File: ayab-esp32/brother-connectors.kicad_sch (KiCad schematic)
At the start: 21 parts, among them J401 900_SOLENOIDS_A, J402 900_SOLENOIDS_B, J403 USER_I2C, J404 USER_SPI, J405 910_SOLENOIDS_A, J406 910_SOLENOIDS_B, J407 910_ENCODERS_EOL_R, J408 USER_UART, J409 930_SOLENOIDS_A, J410 930_SOLENOIDS_B, J411 930_910_EOL_L, J412 930_EOL_R, J413 930_ENCODERS, J414 965_EOL_L, J415 965_EOL_R, J416 965_ENCODERS

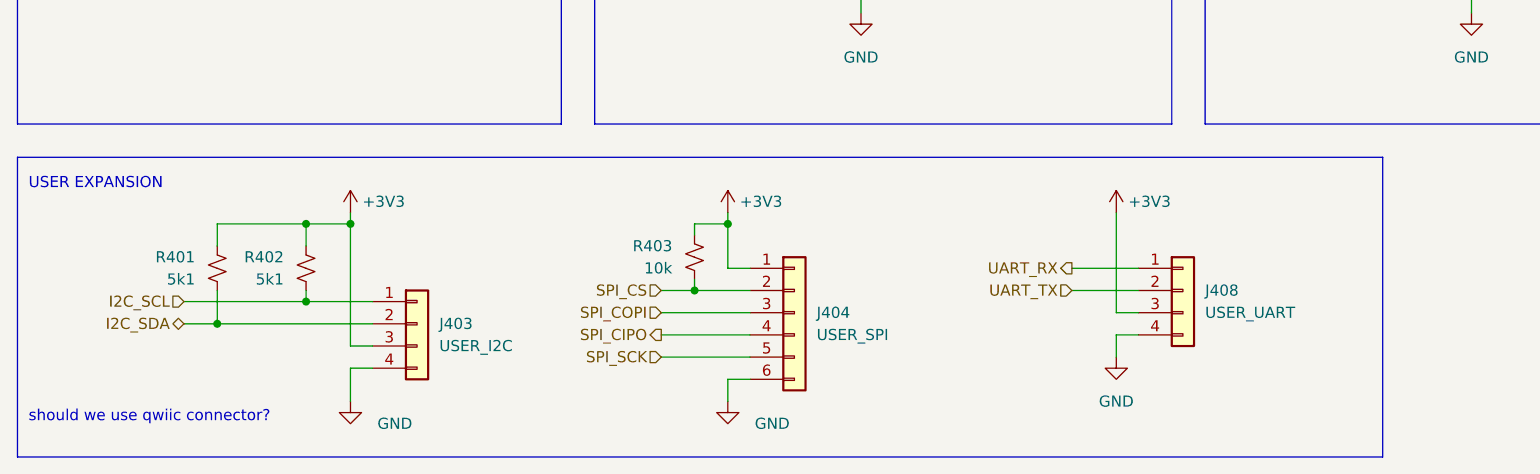
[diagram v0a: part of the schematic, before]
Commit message: bidirectional level shifting
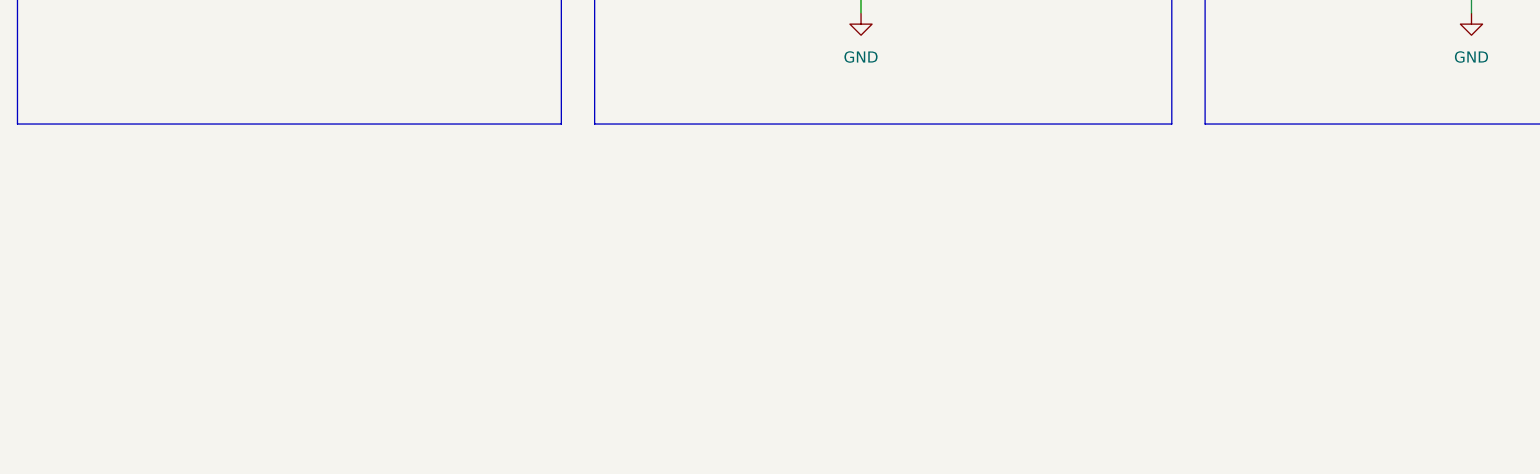
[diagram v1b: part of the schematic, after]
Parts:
- removed J403: USER_I2C, symbol ayab-esp32:Conn_01x04
- removed J404: USER_SPI, symbol ayab-esp32:Conn_01x06
- removed J408: USER_UART, symbol ayab-esp32:Conn_01x04
- removed R401, R402: 5k1, symbol ayab-esp32:R_Small_US
- removed R403: 10k, symbol ayab-esp32:R_Small_US
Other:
- note removed: "USER EXPANSION"
- note removed: "should we use qwiic connector?"

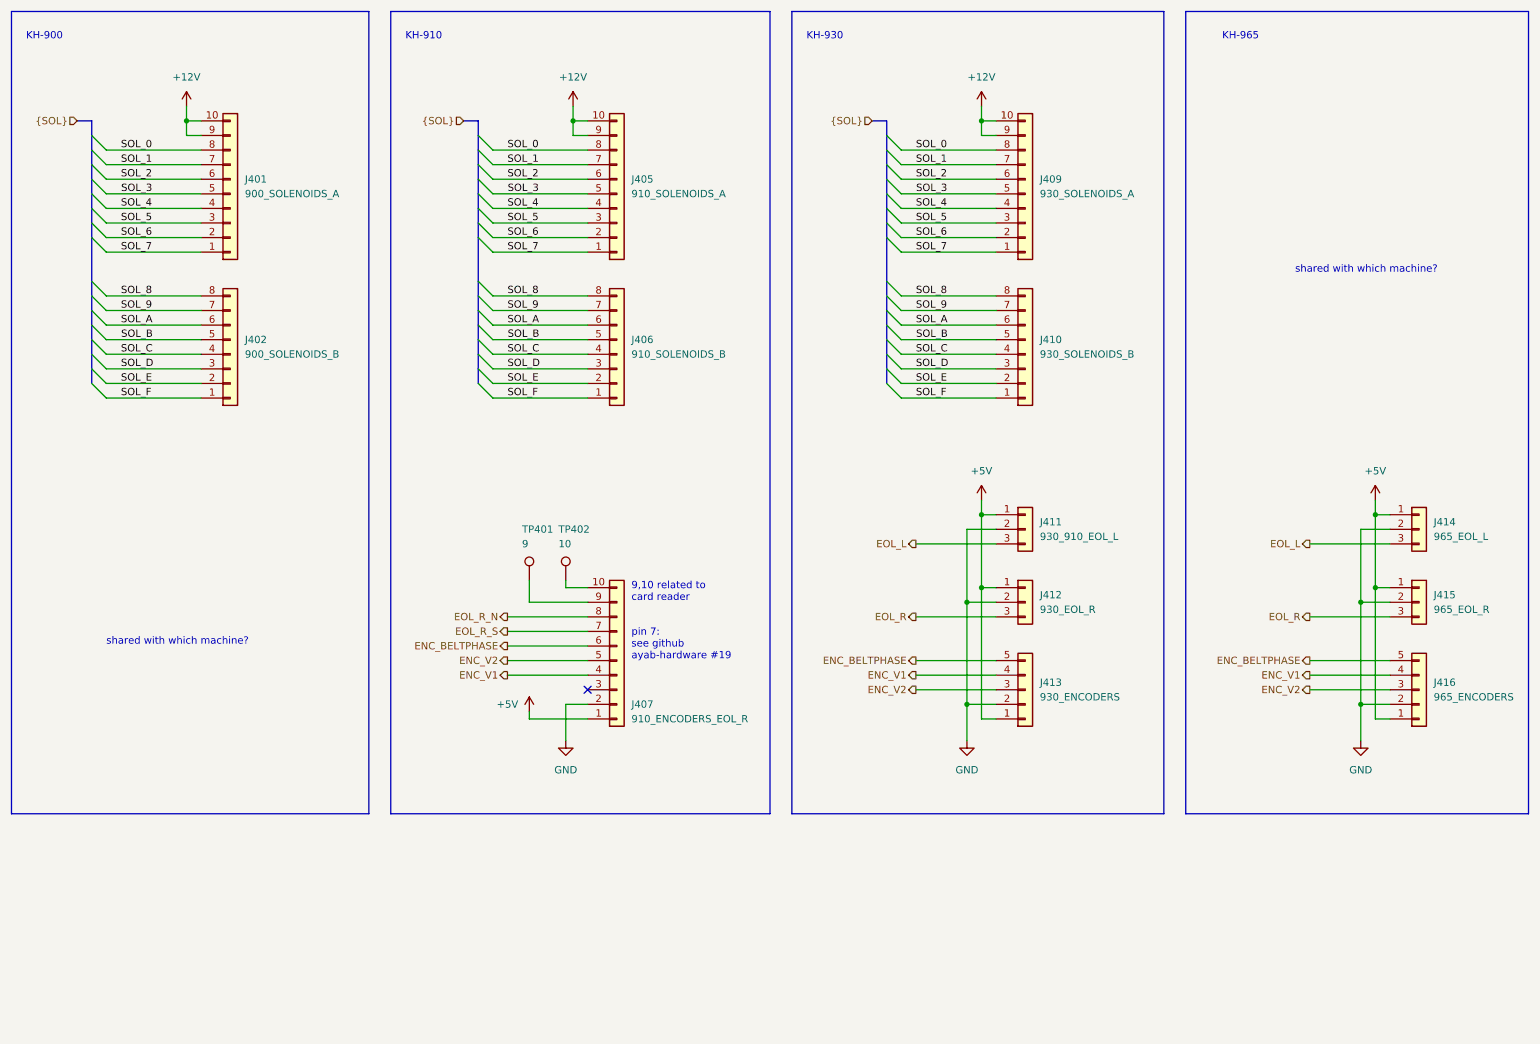
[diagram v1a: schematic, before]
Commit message: annotate and terminating resistors
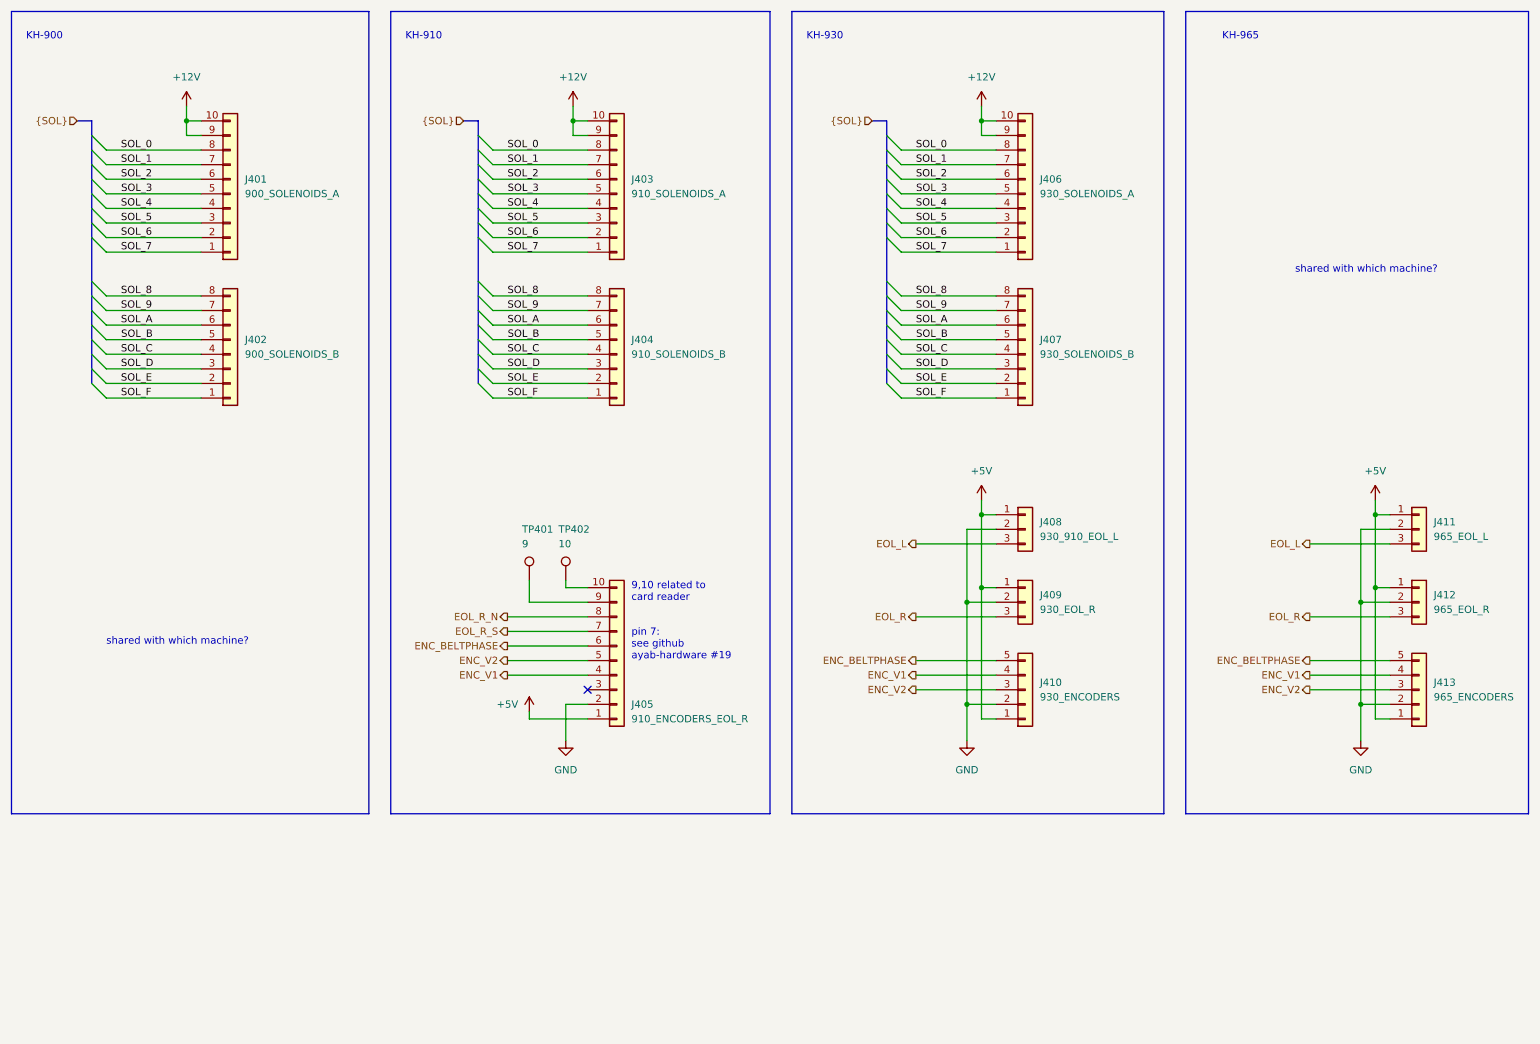
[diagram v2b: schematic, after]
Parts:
- renumbered J405 to J403, J406 to J404, J407 to J405, J409 to J406, J410 to J407, J411 to J408, J412 to J409, J413 to J410, J414 to J411, J415 to J412, J416 to J413

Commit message: add component selection, bom
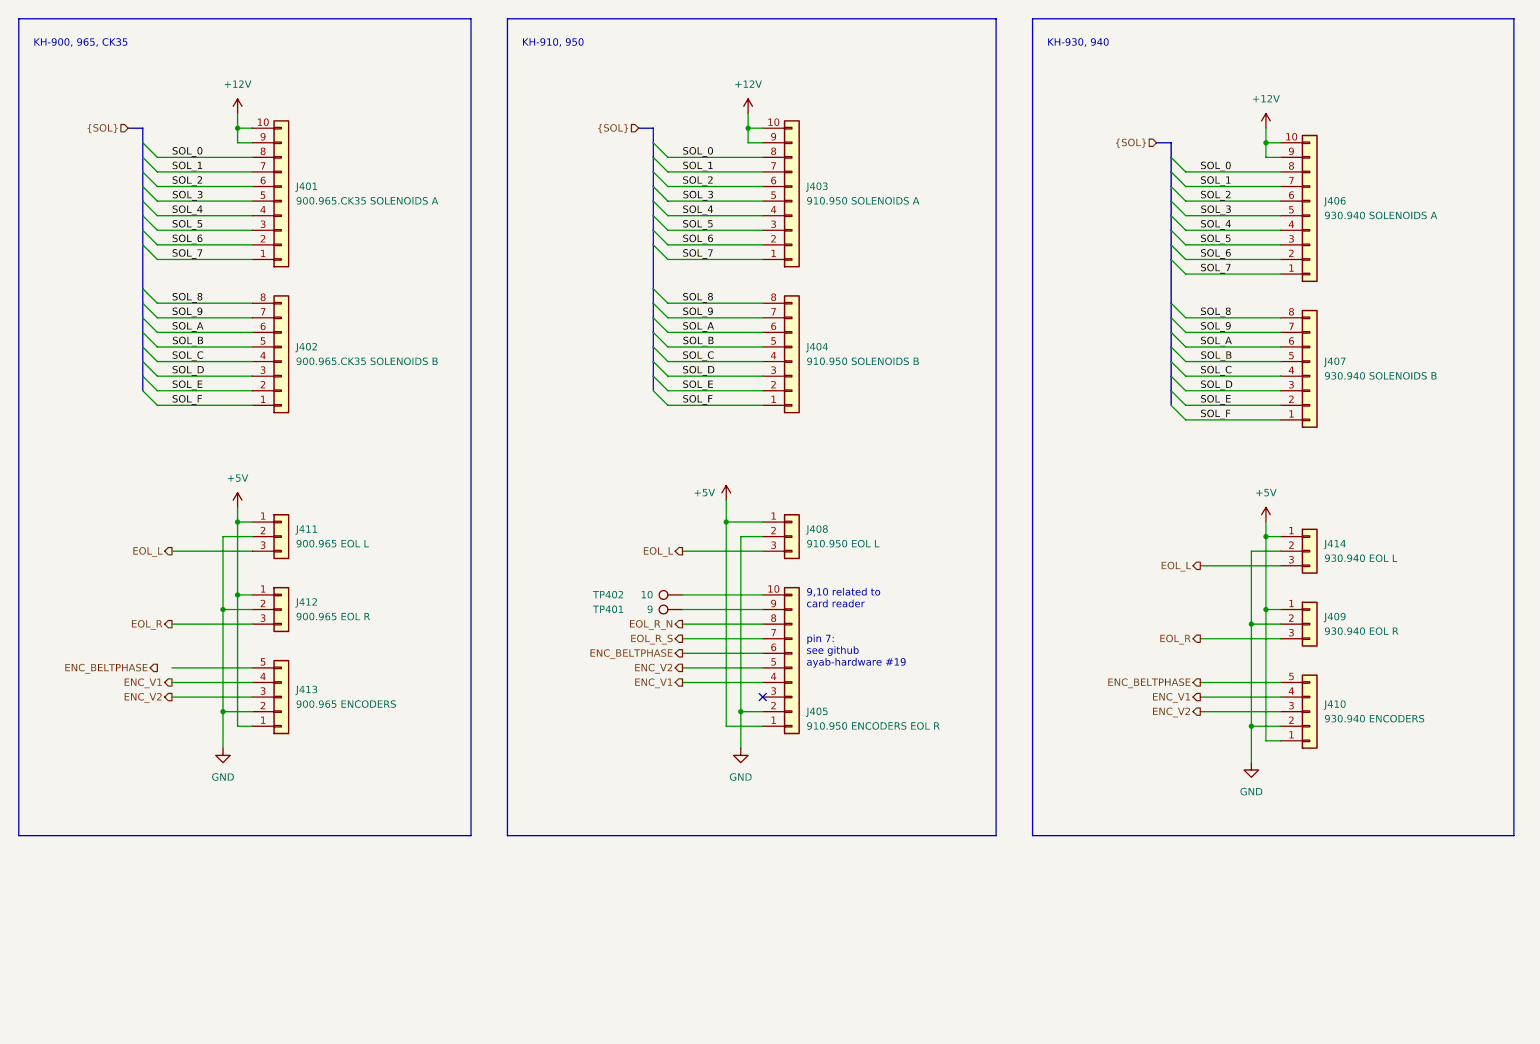
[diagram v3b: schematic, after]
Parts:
- added J414: 930.940 EOL L, easyeda2kicad:CONN-TH_3P-P2.50_X2564WV-03-N0SN, symbol Library:Conn_01x03
- J401: value 900_SOLENOIDS_A -> 900.965.CK35 SOLENOIDS A; footprint (none) -> Library:CONN-TH_CNJMA2004WV-10P; symbol ayab-esp32:Conn_01x10 -> Library:Conn_01x10; LCSC ID (none) -> C2834606; OEM (none) -> CNJM; OEM PN (none) -> CNJMA2004WV-10P
- J402: value 900_SOLENOIDS_B -> 900.965.CK35 SOLENOIDS B; footprint (none) -> Library:CONN-TH_A2004WV-8P; symbol ayab-esp32:Conn_01x08 -> Library:Conn_01x08; LCSC ID (none) -> C225246; OEM (none) -> CJT(Changjiang Connectors); OEM PN (none) -> A2004WV-8P
- J403: value 910_SOLENOIDS_A -> 910.950 SOLENOIDS A; symbol ayab-esp32:Conn_01x10 -> Library:Conn_01x10; OEM (none) -> Hirose; OEM PN (none) -> HNC2-2.5P-10DS(02)
- J404: value 910_SOLENOIDS_B -> 910.950 SOLENOIDS B; symbol ayab-esp32:Conn_01x08 -> Library:Conn_01x08; OEM (none) -> Hirose; OEM PN (none) -> HNC2-2.5P-8DS(02)
- J405: value 910_ENCODERS_EOL_R -> 910.950 ENCODERS EOL R; symbol ayab-esp32:Conn_01x10 -> Library:Conn_01x10; OEM (none) -> Hirose; OEM PN (none) -> HNC2-2.5P-10DS(02)
- J406: value 930_SOLENOIDS_A -> 930.940 SOLENOIDS A; footprint (none) -> Connector_JST:JST_XH_B10B-XH-A_1x10_P2.50mm_Vertical; symbol ayab-esp32:Conn_01x10 -> Library:Conn_01x10; OEM (none) -> HR(Joint Tech Elec); OEM PN (none) -> A2506WV-10P
- J407: value 930_SOLENOIDS_B -> 930.940 SOLENOIDS B; footprint (none) -> easyeda2kicad:CONN-TH_A2506WV-08P; symbol ayab-esp32:Conn_01x08 -> Library:Conn_01x08; LCSC ID (none) -> C476906; OEM (none) -> HR(Joint Tech Elec); OEM PN (none) -> A2506WV-08P
- J408: value 930_910_EOL_L -> 910.950 EOL L; footprint (none) -> Connector_JST:JST_XH_B3B-XH-A_1x03_P2.50mm_Vertical; symbol ayab-esp32:Conn_01x03 -> Library:Conn_01x03; OEM (none) -> Hirose; OEM PN (none) -> HNC2-2.5P-3DS(02)
- J409: value 930_EOL_R -> 930.940 EOL R; footprint (none) -> easyeda2kicad:CONN-TH_3P-P2.50_X2564WV-03-N0SN; symbol ayab-esp32:Conn_01x03 -> Library:Conn_01x03; LCSC ID (none) -> C397419; OEM (none) -> XKB Connectivity; OEM PN (none) -> X2564WV-03-N0SN
- J410: value 930_ENCODERS -> 930.940 ENCODERS; footprint (none) -> easyeda2kicad:CONN-TH_X2564WV-05-N0SN; symbol ayab-esp32:Conn_01x05 -> Library:Conn_01x05; LCSC ID (none) -> C707030; OEM (none) -> XKB Connectivity; OEM PN (none) -> X2564WV-05-N0SN
- J411: value 965_EOL_L -> 900.965 EOL L; footprint (none) -> Library:CONN-TH_3P-P2.00_A2004WV-3P; symbol ayab-esp32:Conn_01x03 -> Library:Conn_01x03; LCSC ID (none) -> C225241; OEM (none) -> CJT(Changjiang Connectors); OEM PN (none) -> A2004WV-3P
- J412: value 965_EOL_R -> 900.965 EOL R; footprint (none) -> Library:CONN-TH_3P-P2.00_A2004WV-3P; symbol ayab-esp32:Conn_01x03 -> Library:Conn_01x03; LCSC ID (none) -> C225241; OEM (none) -> CJT(Changjiang Connectors); OEM PN (none) -> A2004WV-3P
- J413: value 965_ENCODERS -> 900.965 ENCODERS; footprint (none) -> Library:CONN-TH_A2004WV-5P; symbol ayab-esp32:Conn_01x05 -> Library:Conn_01x05; LCSC ID (none) -> C225243; OEM (none) -> CJT(Changjiang Connectors); OEM PN (none) -> A2004WV-5P
- TP401, TP402: footprint (none) -> TestPoint:TestPoint_Pad_D2.0mm; symbol ayab-esp32:TestPoint -> Library:TestPoint; now left out of the parts list
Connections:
- net +5V: now also J414.1 (Pin_1)
- net ENC_BELTPHASE: no longer J413.5 (Pin_5)
- net EOL_L: now also J414.3 (Pin_3)
- net GND: now also J414.2 (Pin_2)
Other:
- note added: "KH-900, 965, CK35"
- note added: "KH-910, 950"
- note added: "KH-930, 940"
- note removed: "KH-900"
- note removed: "KH-910"
- note removed: "KH-930"
- note removed: "KH-965"
- note removed: "shared with which machine?"
- moved on the sheet: J401, J402, J403, J404, J405, J406, J407, J408, J409, J410, J411, J412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
